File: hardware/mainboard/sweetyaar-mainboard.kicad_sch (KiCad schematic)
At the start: 100 parts, among them Q1 MMBT3904

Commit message: Adding routing to PCB design
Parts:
- removed TP12: ${SHORT_NET_NAME(1)}, TestPoint:TestPoint_Pad_D2.0mm, symbol Connector:TestPoint
- added C_MUX4: 1uF, 25 V, X7R, ±10%, Capacitor_SMD:C_0603_1608Metric, symbol Device:C
- D_LED1: symbol LCSC:WS2812B-V6 -> SweetYaar:WS2812B-V6
- renumbered C17 to C_3V3_IN1, C2 to C_3V3_OUT1, C_3V3_IN1 to C_5V_IN1
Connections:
- net 5V_INPUT: now also C_MUX4.1
- net GND: now also C_MUX4.2
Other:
- note removed: "Test points to allow easy connection of later added additional LEDs."
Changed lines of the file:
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@@
 		)
 	)
-	(text "Test points to allow easy connection \nof later added additional LEDs."
-		(exclude_from_sim no)
-		(at 376.682 214.122 0)
-		(effects
-			(font
-				(size 1.27 1.27)
-			)
-			(justify left)
-		)
-	)
 	(text "Charging Module"
 		(exclude_from_sim no)
@@
 	)
 	(junction
-		(at 248.92 243.84)
-		(diameter 0)
-		(color 0 0 0 0)
-	)
-	(junction
 		(at 217.17 116.84)
 		(diameter 0)
@@
 	)
 	(junction
+		(at 144.78 72.39)
+		(diameter 0)
+		(color 0 0 0 0)
+	)
+	(junction
 		(at 336.55 120.65)
 		(diameter 0)
@@
 		(color 0 0 0 0)
 	)
+	(junction
+		(at 149.86 72.39)
+		(diameter 0)
+		(color 0 0 0 0)
+	)
 	(no_connect
 		(at 60.96 74.93)
@@
 	(wire
 		(pts
+			(xy 149.86 72.39) (xy 144.78 72.39)
+		)
+		(stroke
+			(width 0)
+			(type default)
+		)
+	)
+	(wire
+		(pts
 			(xy 283.21 233.68) (xy 283.21 231.14)
 		)
@@
 	(wire
 		(pts
+			(xy 152.4 72.39) (xy 149.86 72.39)
+		)
+		(stroke
+			(width 0)
+			(type default)
+		)
+	)
+	(wire
+		(pts
 			(xy 92.71 62.23) (xy 92.71 58.42)
 		)
@@
 	)
 	(label "5V_INPUT"
-		(at 144.78 72.39 0)
+		(at 152.4 72.39 0)
 		(effects
 			(font
@@
 	)
 	(symbol
-		(lib_id "LCSC:WS2812B-V6")
+		(lib_id "SweetYaar:WS2812B-V6")
 		(at 342.9 223.52 0)
 		(unit 1)
@@
 		(in_pos_files yes)
 		(dnp no)
-		(property "Reference" "C_3V3_IN1"
+		(property "Reference" "C_5V_IN1"
 			(at 283.21 106.68 0)
 			(hide yes)
@@
 			(project "sweetyaar-mainboard"
 				(path "/a2bc0001-0000-4000-8000-000000000001"
-					(reference "C_3V3_IN1")
+					(reference "C_5V_IN1")
 					(unit 1)
 				)
@@
 	)
 	(symbol
+		(lib_id "power:GND")
+		(at 149.86 80.01 0)
+		(unit 1)
+		(body_style 1)
+		(exclude_from_sim no)
+		(in_bom yes)
+		(on_board yes)
+		(in_pos_files yes)
+		(dnp no)
+		(property "Reference" "#PWR08"
+			(at 149.86 80.01 0)
+			(hide yes)
+			(show_name no)
+			(do_not_autoplace no)
+			(effects
+				(font
+					(size 1.27 1.27)
+				)
+			)
+		)
+		(property "Value" "GND"
+			(at 150.114 83.82 0)
+			(show_name no)
+			(do_not_autoplace no)
+			(effects
+				(font
+					(size 1.27 1.27)
+				)
+			)
+		)
+		(property "Footprint" ""
+			(at 149.86 80.01 0)
+			(show_name no)
+			(do_not_autoplace no)
+			(effects
+				(font
+					(size 1.27 1.27)
+				)
+			)
+		)
+		(property "Datasheet" ""
+			(at 149.86 80.01 0)
+			(show_name no)
+			(do_not_autoplace no)
+			(effects
+				(font
+					(size 1.27 1.27)
+				)
+			)
+		)
+		(property "Description" ""
+			(at 149.86 80.01 0)
+			(show_name no)
+			(do_not_autoplace no)
+			(effects
+				(font
+					(size 1.27 1.27)
+				)
+			)
+		)
+		(pin "1"
+		)
+		(instances
+			(project "sweetyaar-mainboard"
+				(path "/a2bc0001-0000-4000-8000-000000000001"
+					(reference "#PWR08")
+					(unit 1)
+				)
+			)
+		)
+	)
+	(symbol
 		(lib_id "Device:R")
 		(at 252.73 256.54 90)
@@
 		(in_pos_files yes)
 		(dnp no)
-		(fields_autoplaced yes)
 		(property "Reference" "JP3"
 			(at 210.82 121.92 0)
@@
 	)
 	(symbol
+		(lib_id "Device:C")
+		(at 149.86 76.2 0)
+		(unit 1)
+		(body_style 1)
+		(exclude_from_sim no)
+		(in_bom yes)
+		(on_board yes)
+		(in_pos_files yes)
+		(dnp no)
+		(property "Reference" "C_MUX4"
+			(at 151.13 73.66 0)
+			(hide yes)
+			(show_name no)
+			(do_not_autoplace no)
+			(effects
+				(font
+					(size 1.27 1.27)
+				)
+			)
+		)
+		(property "Value" "1uF, 25 V, X7R, ±10%"
+			(at 154.432 74.168 0)
+			(show_name no)
+			(do_not_autoplace no)
+			(effects
+				(font
+					(size 1.27 1.27)
+				)
+			)
+		)
+		(property "Footprint" "Capacitor_SMD:C_0603_1608Metric"
+			(at 149.86 76.2 0)
+			(hide yes)
+			(show_name no)
+			(do_not_autoplace no)
+			(effects
+				(font
+					(size 1.27 1.27)
+				)
+			)
+		)
+		(property "Datasheet" ""
+			(at 149.86 76.2 0)
+			(hide yes)
+			(show_name no)
+			(do_not_autoplace no)
+			(effects
+				(font
+					(size 1.27 1.27)
+				)
+			)
+		)
+		(property "Description" ""
+			(at 149.86 76.2 0)
+			(show_name no)
+			(do_not_autoplace no)
+			(effects
+				(font
+					(size 1.27 1.27)
+				)
+			)
+		)
+		(property "LCSC" "C29936"
+			(at 149.86 76.2 0)
+			(hide yes)
+			(show_name no)
+			(do_not_autoplace no)
+			(effects
+				(font
+					(size 1.27 1.27)
+				)
+			)
+		)
+		(property "FT Rotation Offset" ""
+			(at 149.86 76.2 0)
+			(hide yes)
+			(show_name no)
+			(do_not_autoplace no)
+			(effects
+				(font
+					(size 1.27 1.27)
+				)
+			)
+		)
+		(property "Sim.Device" ""
+			(at 149.86 76.2 0)
+			(hide yes)
+			(show_name no)
+			(do_not_autoplace no)
+			(effects
+				(font
+					(size 1.27 1.27)
+				)
+			)
+		)
+		(property "Sim.Pins" ""
+			(at 149.86 76.2 0)
+			(hide yes)
+			(show_name no)
+			(do_not_autoplace no)
+			(effects
+				(font
+					(size 1.27 1.27)
+				)
+			)
+		)
+		(pin "1"
+		)
+		(pin "2"
+		)
+		(instances
+			(project "sweetyaar-mainboard"
+				(path "/a2bc0001-0000-4000-8000-000000000001"
+					(reference "C_MUX4")
+					(unit 1)
+				)
+			)
+		)
+	)
+	(symbol
 		(lib_id "power:GND")
 		(at 57.15 163.83 0)
@@
 		(in_pos_files yes)
 		(dnp no)
-		(property "Reference" "C17"
+		(property "Reference" "C_3V3_IN1"
 			(at 285.75 66.04 0)
 			(hide yes)
@@
 			(project "sweetyaar-mainboard"
 				(path "/a2bc0001-0000-4000-8000-000000000001"
-					(reference "C17")
+					(reference "C_3V3_IN1")
 					(unit 1)
 				)
@@
 		(in_pos_files yes)
 		(dnp no)
-		(property "Reference" "C2"
+		(property "Reference" "C_3V3_OUT1"
 			(at 337.82 66.04 0)
 			(hide yes)
@@
 			(project "sweetyaar-mainboard"
 				(path "/a2bc0001-0000-4000-8000-000000000001"
-					(reference "C2")
+					(reference "C_3V3_OUT1")
 					(unit 1)
 				)
@@
 					(unit 1)
 				)
-			)
-		)
-	)
-	(symbol
-		(lib_id "Connector:TestPoint")
-		(at 248.92 243.84 270)
-		(unit 1)
-		(body_style 1)
-		(exclude_from_sim no)
-		(in_bom no)
-		(on_board yes)
-		(in_pos_files no)
-		(dnp no)
-		(property "Reference" "TP12"
-			(at 254 242.316 0)
-			(show_name no)
-			(do_not_autoplace no)
-			(effects
-				(font
-					(size 1.27 1.27)
-				)
-				(justify left)
-			)
-		)
-		(property "Value" "${SHORT_NET_NAME(1)}"
-			(at 250.9521 246.38 0)
-			(hide yes)
-			(show_name no)
-			(do_not_autoplace no)
-			(effects
-				(font
-					(size 1.27 1.27)
-				)
-				(justify left)
-			)
-		)
-		(property "Footprint" "TestPoint:TestPoint_Pad_D2.0mm"
-			(at 248.92 248.92 0)
-			(hide yes)
-			(show_name no)
-			(do_not_autoplace no)
-			(effects
-				(font
-					(size 1.27 1.27)
-				)
-			)
-		)
-		(property "Datasheet" ""
-			(at 248.92 248.92 0)
-			(hide yes)
-			(show_name no)
-			(do_not_autoplace no)
-			(effects
-				(font
-					(size 1.27 1.27)
-				)
-			)
-		)
-		(property "Description" "test point"
-			(at 248.92 243.84 0)
-			(hide yes)
-			(show_name no)
-			(do_not_autoplace no)
-			(effects
-				(font
-					(size 1.27 1.27)
-				)
-			)
-		)
-		(property "FT Rotation Offset" ""
-			(at 248.92 243.84 0)
-			(hide yes)
-			(show_name no)
-			(do_not_autoplace no)
-			(effects
-				(font
-					(size 1.27 1.27)
-				)
-			)
-		)
-		(property "Sim.Device" ""
-			(at 248.92 243.84 0)
-			(hide yes)
-			(show_name no)
-			(do_not_autoplace no)
-			(effects
-				(font
-					(size 1.27 1.27)
-				)
-			)
-		)
-		(property "Sim.Pins" ""
-			(at 248.92 243.84 0)
-			(hide yes)
-			(show_name no)
-			(do_not_autoplace no)
-			(effects
-				(font
-					(size 1.27 1.27)
-				)
-			)
-		)
-		(pin "1"
-		)
-		(instances
-			(project "sweetyaar-mainboard"
-				(path "/a2bc0001-0000-4000-8000-000000000001"
-					(reference "TP12")
-					(unit 1)
-				)

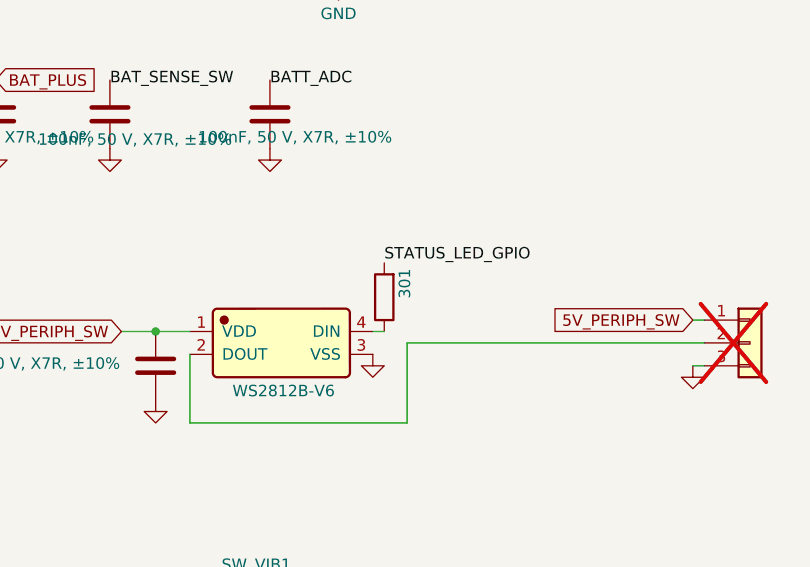
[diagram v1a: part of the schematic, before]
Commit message: Moving LED to the edge of the board
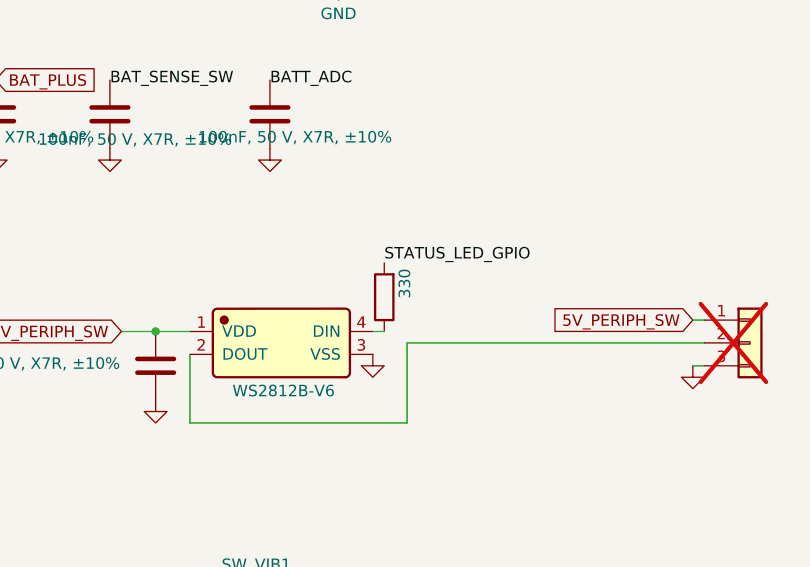
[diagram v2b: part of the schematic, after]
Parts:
- R_LED_DIN1: value 301 -> 330; LCSC C25192 -> C23138
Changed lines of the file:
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@@
 			)
 		)
-		(property "Value" "301"
+		(property "Value" "330"
 			(at 356.616 216.916 90)
 			(show_name no)
@@
 			)
 		)
-		(property "Datasheet" ""
+		(property "Datasheet" "https://www.lcsc.com/datasheet/C23138.pdf"
 			(at 354.33 218.44 0)
 			(hide yes)
@@
 			)
 		)
-		(property "Description" ""
+		(property "Description" "330 Ohm, +/-1%, 100mW, 0603 thick film resistor"
 			(at 354.33 218.44 0)
+			(hide yes)
 			(show_name no)
 			(do_not_autoplace no)
@@
 			)
 		)
-		(property "LCSC" "C25192"
+		(property "LCSC" "C23138"
 			(at 354.33 218.44 90)
 			(hide yes)

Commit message: Fixing rotation and position offsets
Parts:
- J_USB1: footprint SweetYaar:USB_C_Receptacle_HRO_TYPE-C-31-M-12 -> SweetYaar:USB_C_Receptacle_HRO_TYPE-C-31-M-12 - C165948
- U_AMP1: footprint SweetYaar:TQFN-16-1EP_3x3mm_P0.5mm_EP1.23x1.23mm -> SweetYaar:TQFN-16-1EP_3x3mm_P0.5mm_EP1.23x1.23mm - C910544
- U_ESP32: footprint RF_Module:ESP32-WROOM-32E -> SweetYaar:ESP32-WROOM-32E - C701342
- U_MUX1: footprint Package_TO_SOT_SMD:SOT-583-8 -> SweetYaar:SOT-583-8 - C3235557
- U_SW_BAT1, U_SW_SD1: footprint Package_TO_SOT_SMD:SOT-23-6 -> SweetYaar:SOT-23-6 - C128634
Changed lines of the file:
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@@
 			)
 		)
-		(property "Footprint" "Package_TO_SOT_SMD:SOT-23-6"
+		(property "Footprint" "SweetYaar:SOT-23-6 - C128634"
 			(at 378.46 81.28 0)
 			(hide yes)
@@
 			)
 		)
-		(property "FT Rotation Offset" ""
-			(at 378.46 81.28 0)
-			(hide yes)
-			(show_name no)
-			(do_not_autoplace no)
-			(effects
-				(font
-					(size 1.27 1.27)
-				)
-			)
-		)
 		(property "Sim.Device" ""
 			(at 378.46 81.28 0)
@@
 			)
 		)
-		(property "Footprint" "SweetYaar:USB_C_Receptacle_HRO_TYPE-C-31-M-12"
+		(property "Footprint" "SweetYaar:USB_C_Receptacle_HRO_TYPE-C-31-M-12 - C165948"
 			(at 49.53 77.47 0)
 			(hide yes)
@@
 			)
 		)
-		(property "Footprint" "Package_TO_SOT_SMD:SOT-583-8"
+		(property "Footprint" "SweetYaar:SOT-583-8 - C3235557"
 			(at 134.62 77.47 0)
 			(hide yes)
@@
 			)
 		)
-		(property "Footprint" "Package_TO_SOT_SMD:SOT-23-6"
+		(property "Footprint" "SweetYaar:SOT-23-6 - C128634"
 			(at 328.93 173.99 0)
 			(hide yes)
@@
 			)
 		)
-		(property "FT Rotation Offset" ""
-			(at 328.93 173.99 0)
-			(hide yes)
-			(show_name no)
-			(do_not_autoplace no)
-			(effects
-				(font
-					(size 1.27 1.27)
-				)
-			)
-		)
 		(property "Sim.Device" ""
 			(at 328.93 173.99 0)
@@
 			)
 		)
-		(property "Footprint" "RF_Module:ESP32-WROOM-32E"
+		(property "Footprint" "SweetYaar:ESP32-WROOM-32E - C701342"
 			(at 248.92 208.28 0)
 			(hide yes)
@@
 			)
 		)
-		(property "FT Rotation Offset" ""
-			(at 248.92 208.28 0)
-			(hide yes)
-			(show_name no)
-			(do_not_autoplace no)
-			(effects
-				(font
-					(size 1.27 1.27)
-				)
-			)
-		)
 		(property "Sim.Device" ""
 			(at 248.92 208.28 0)
@@
 			)
 		)
-		(property "Footprint" "SweetYaar:TQFN-16-1EP_3x3mm_P0.5mm_EP1.23x1.23mm"
+		(property "Footprint" "SweetYaar:TQFN-16-1EP_3x3mm_P0.5mm_EP1.23x1.23mm - C910544"
 			(at 157.48 246.38 0)
 			(hide yes)

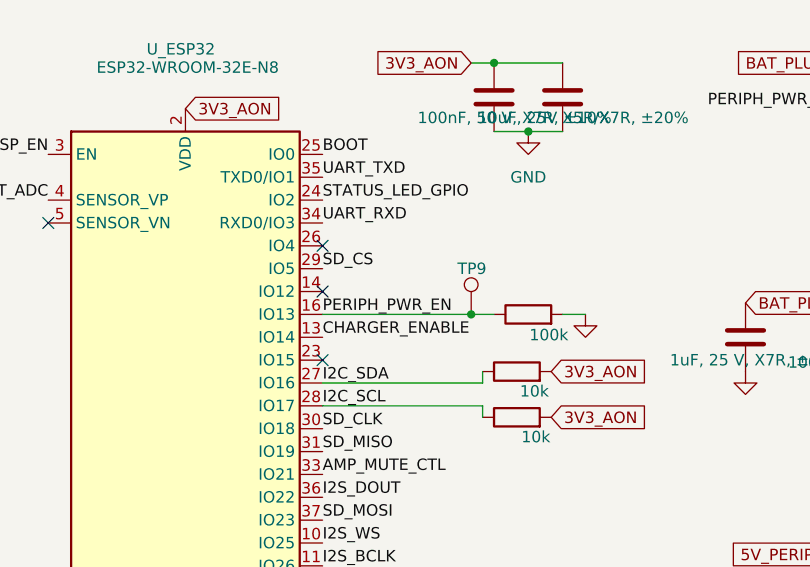
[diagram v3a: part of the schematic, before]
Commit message: Changing CHARGING_ENABLE to GPIO4
previous GPIO was held down momentarily on reset by the ESP and this could potentially allow charging without finishing setting up battery profile.
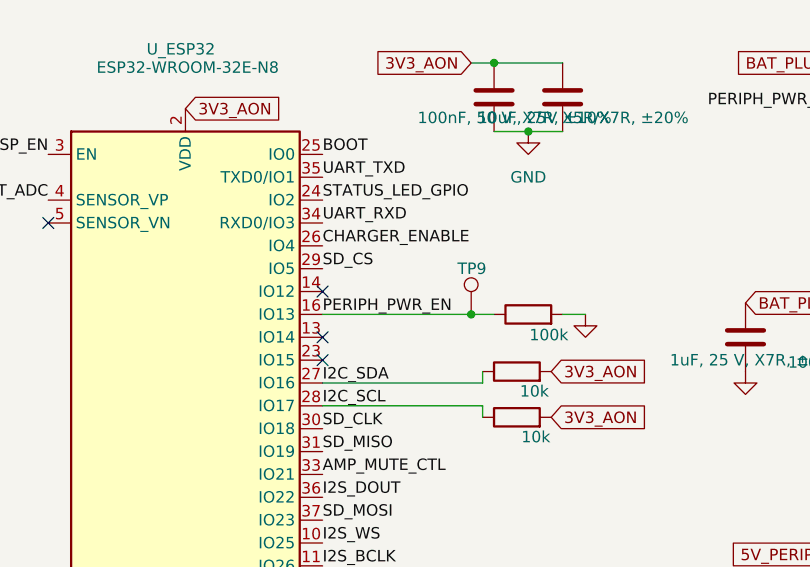
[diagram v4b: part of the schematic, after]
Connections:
- net CHARGER_ENABLE: now also U_ESP32.26 (IO4); no longer U_ESP32.13 (IO14)
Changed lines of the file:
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@@
 	)
 	(no_connect
-		(at 264.16 187.96)
+		(at 264.16 198.12)
 	)
 	(no_connect
@@
 	)
 	(label "CHARGER_ENABLE"
-		(at 264.16 198.12 0)
-		(effects
-			(font
+		(at 264.16 187.96 0)
+		(effects
+			(font

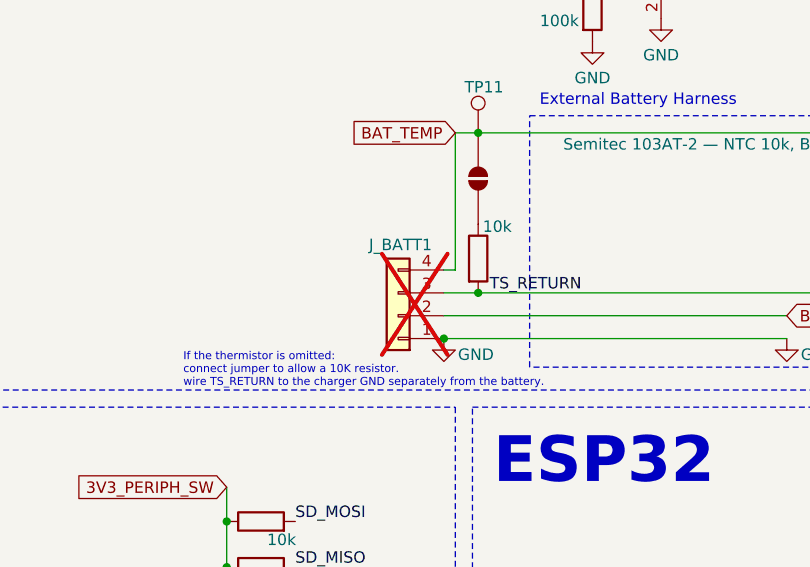
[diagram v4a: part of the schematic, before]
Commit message: changing battery connector to 5 pins (one unused) for better protection against assembly mistakes
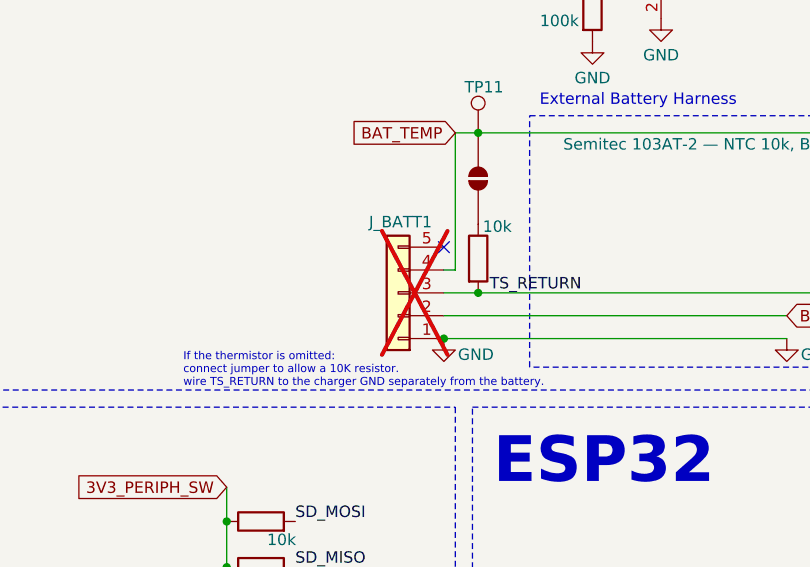
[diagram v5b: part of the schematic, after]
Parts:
- J_BATT1: footprint Connector_JST:JST_XH_B4B-XH-A_1x04_P2.50mm_Vertical -> (none); symbol Connector_Generic:Conn_01x04 -> Connector_Generic:Conn_01x05; LCSC C144395 -> (none)
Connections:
- no-connect marks 15 -> 16
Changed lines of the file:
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@@
 	)
 	(no_connect
+		(at 213.36 129.54)
+	)
+	(no_connect
 		(at 144.78 82.55)
 	)
@@
 	)
 	(symbol
-		(lib_id "Connector_Generic:Conn_01x04")
-		(at 208.28 137.16 180)
+		(lib_id "Connector_Generic:Conn_01x05")
+		(at 208.28 134.62 180)
 		(unit 1)
 		(body_style 1)
@@
 		(dnp yes)
 		(property "Reference" "J_BATT1"
-			(at 208.534 129.286 0)
+			(at 208.534 126.746 0)
 			(show_name no)
 			(do_not_autoplace no)
@@
 		)
 		(property "Value" "BAT JST-XH"
-			(at 207.01 134.62 0)
+			(at 207.01 132.08 0)
 			(hide yes)
 			(show_name no)
@@
 			)
 		)
-		(property "Footprint" "Connector_JST:JST_XH_B4B-XH-A_1x04_P2.50mm_Vertical"
-			(at 208.28 137.16 0)
+		(property "Footprint" ""
+			(at 208.28 134.62 0)
 			(hide yes)
 			(show_name no)
@@
 		)
 		(property "Datasheet" ""
-			(at 208.28 137.16 0)
+			(at 208.28 134.62 0)
 			(hide yes)
 			(show_name no)
@@
 			)
 		)
-		(property "Description" "Generic connector, single row, 01x04, script generated (kicad-library-utils/schlib/autogen/connector/)"
-			(at 208.28 137.16 0)
-			(hide yes)
-			(show_name no)
-			(do_not_autoplace no)
-			(effects
-				(font
-					(size 1.27 1.27)
-				)
-			)
-		)
-		(property "LCSC" "C144395"
-			(at 208.28 137.16 0)
+		(property "Description" "Generic connector, single row, 01x05, script generated (kicad-library-utils/schlib/autogen/connector/)"
+			(at 208.28 134.62 0)
 			(hide yes)
 			(show_name no)
@@
 		(pin "4"
 		)
+		(pin "5"
+		)
 		(instances

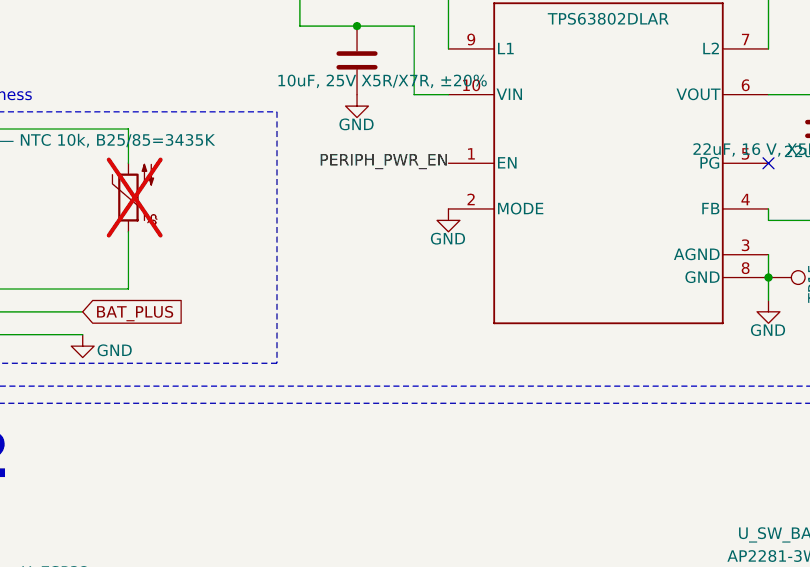
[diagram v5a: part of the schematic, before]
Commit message: Adding a solder jumper (open) to allow changing 5V regulator MODE to PWM.
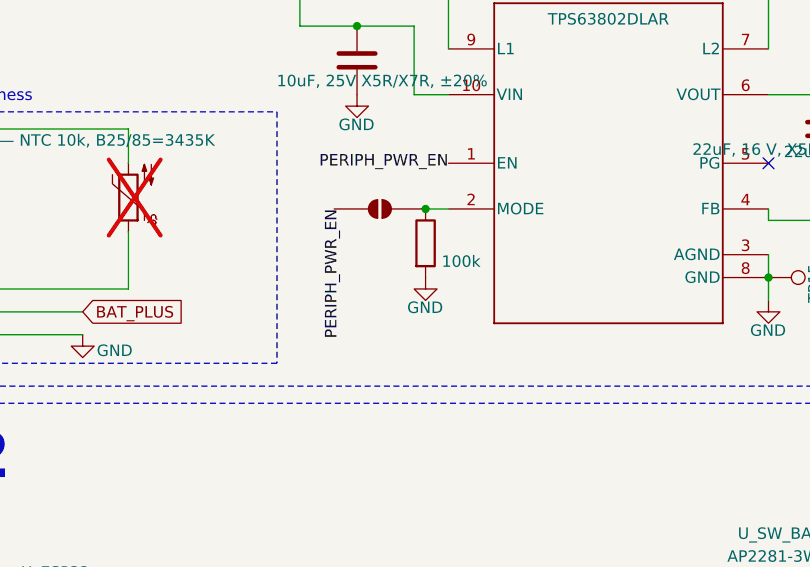
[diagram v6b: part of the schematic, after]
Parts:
- added JP4: SolderJumper_2_Open, Jumper:SolderJumper-2_P1.3mm_Open_RoundedPad1.0x1.5mm, symbol Jumper:SolderJumper_2_Open
- added R_MODE_PD1: 100k, Resistor_SMD:R_0603_1608Metric, symbol Device:R
- J_BATT1: footprint (none) -> Connector_JST:JST_XH_B5B-XH-A_1x05_P2.50mm_Vertical
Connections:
- net GND: now also R_MODE_PD1.2; no longer U_5V1.2 (MODE)
- net PERIPH_PWR_EN: now also JP4.1 (A)
- new net: JP4.2 (B), R_MODE_PD1.1, U_5V1.2 (MODE)
